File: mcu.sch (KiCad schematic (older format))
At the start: 45 parts, among them J10 debug, J7 PE10-15, J8 PD0-7, J9 USB_C_Receptacle_USB2.0, SW1 SW_MEC_5E, SW2 SW_MEC_5E, U3 STM32F407VETx, Y1 12.228Mhz

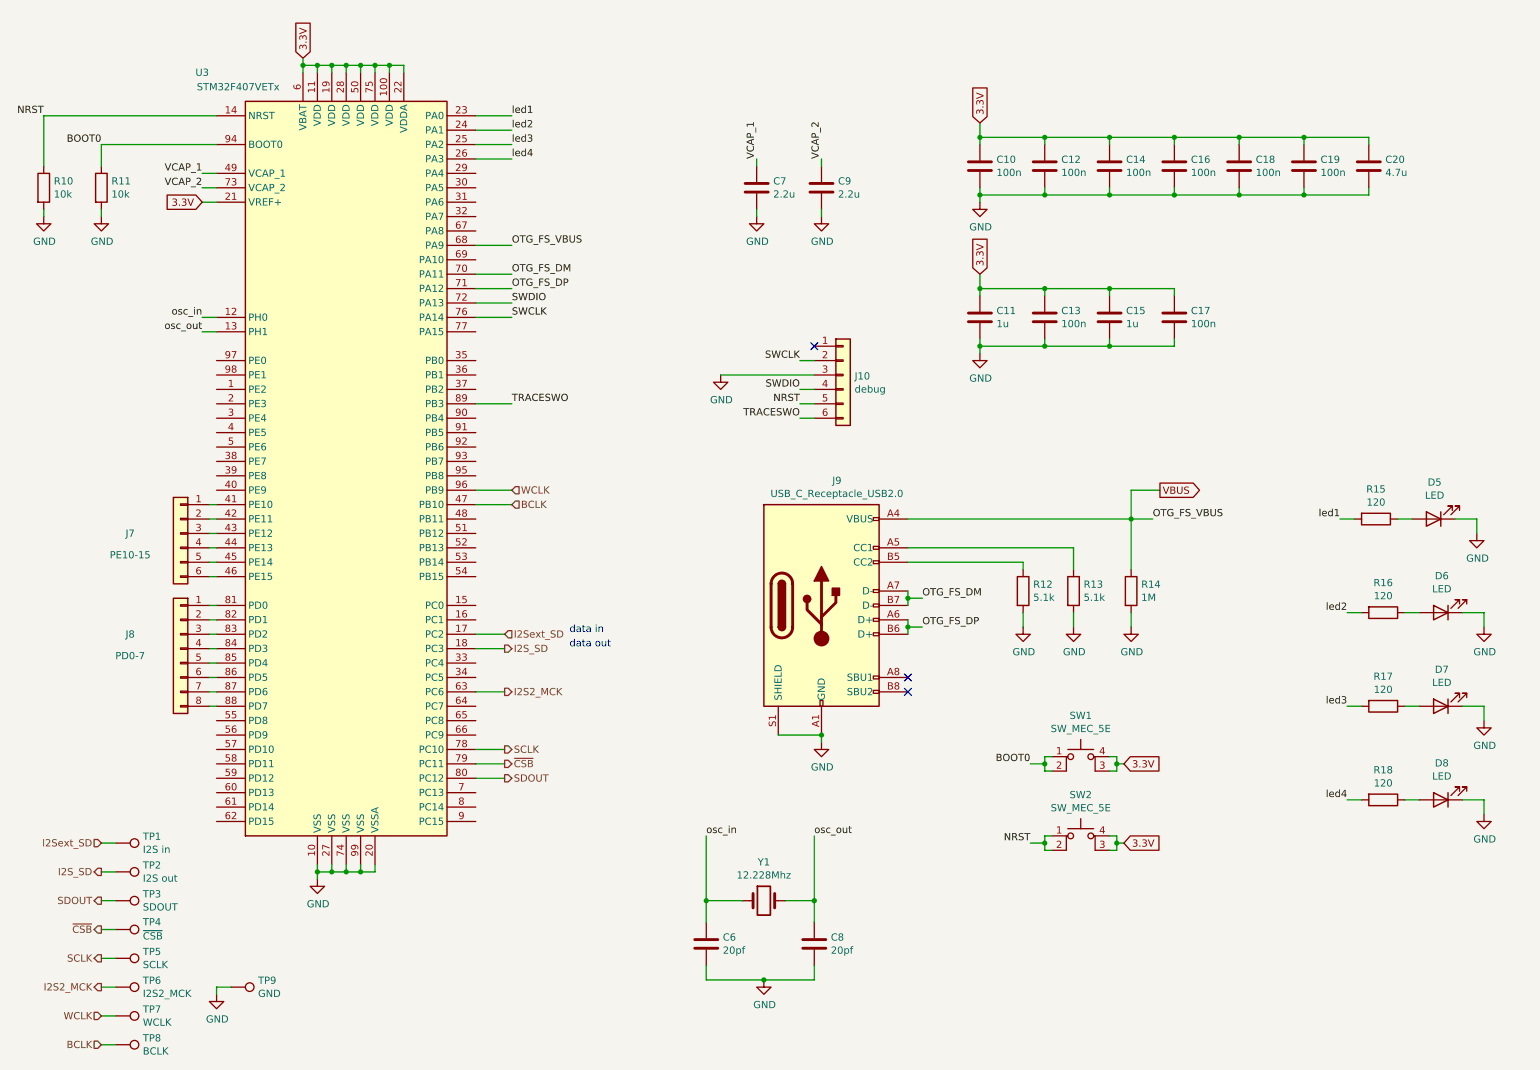
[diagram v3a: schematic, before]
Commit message: Improved probe points
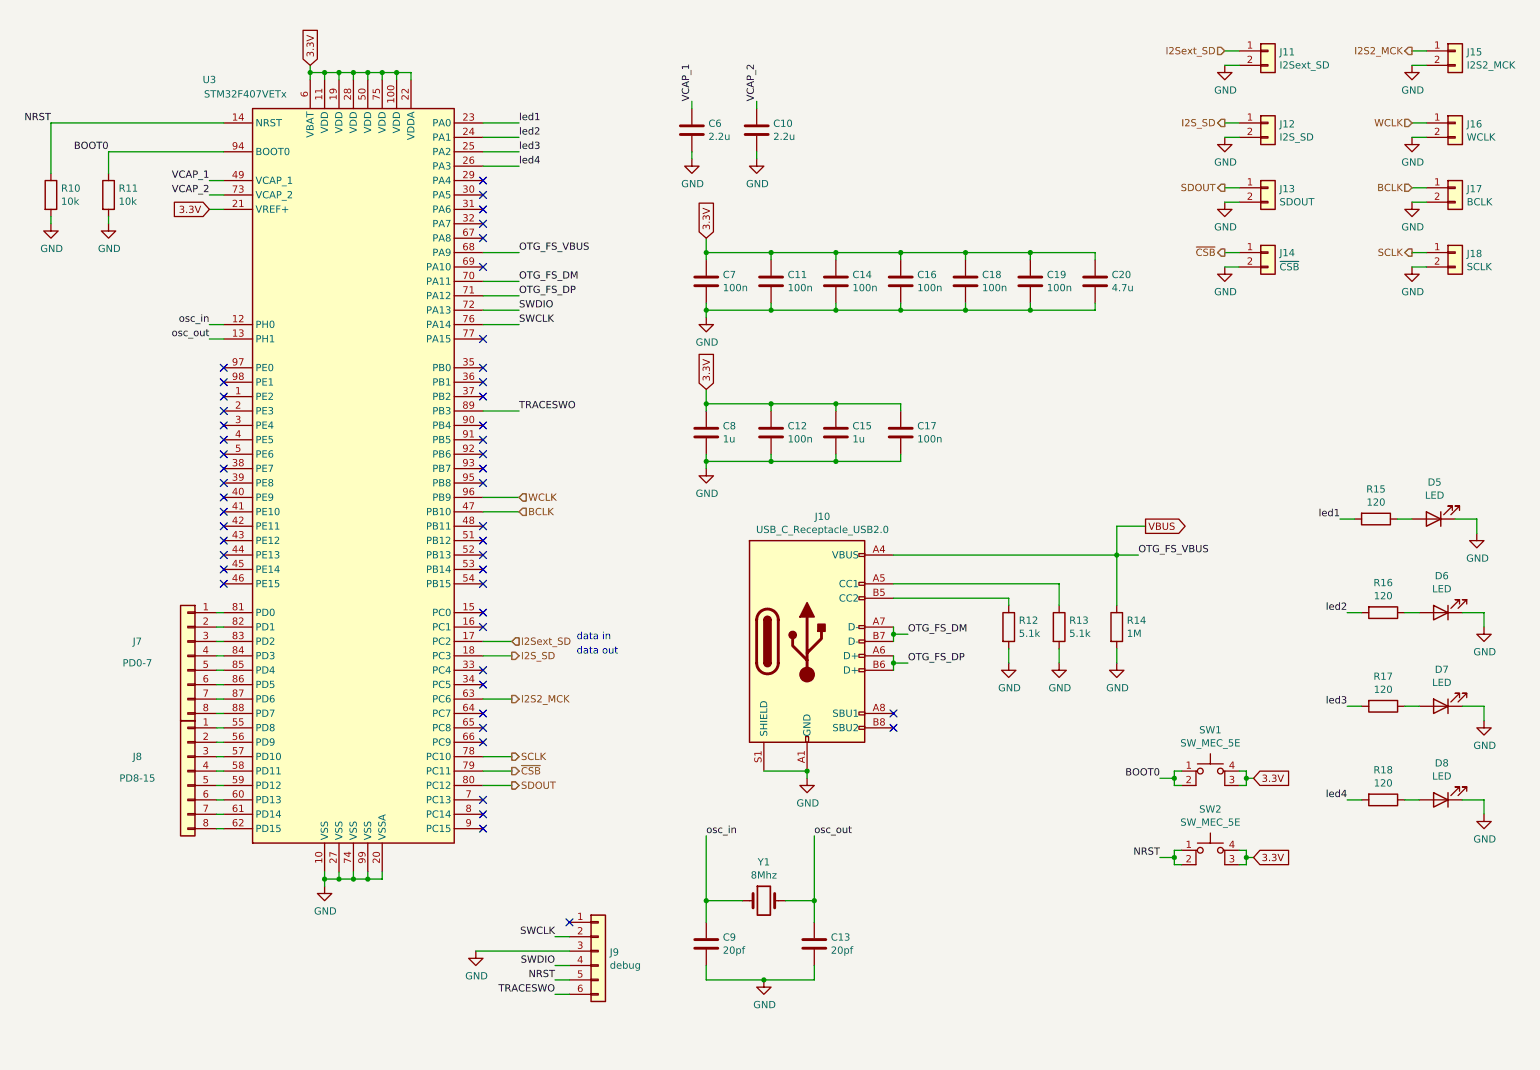
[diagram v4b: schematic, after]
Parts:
- removed J7: PE10-15, symbol Connector_Generic:Conn_01x06
- removed TP1: I2S in, symbol Connector:TestPoint
- removed TP2: I2S out, symbol Connector:TestPoint
- removed TP3: SDOUT, symbol Connector:TestPoint
- removed TP4: ~CSB, symbol Connector:TestPoint
- removed TP5: SCLK, symbol Connector:TestPoint
- removed TP6: I2S2_MCK, symbol Connector:TestPoint
- removed TP7: WCLK, symbol Connector:TestPoint
- removed TP8: BCLK, symbol Connector:TestPoint
- removed TP9: GND, symbol Connector:TestPoint
- added J11: I2Sext_SD, symbol Connector_Generic:Conn_01x02
- added J12: I2S_SD, symbol Connector_Generic:Conn_01x02
- added J13: SDOUT, symbol Connector_Generic:Conn_01x02
- added J14: ~CSB, symbol Connector_Generic:Conn_01x02
- added J15: I2S2_MCK, symbol Connector_Generic:Conn_01x02
- added J16: WCLK, symbol Connector_Generic:Conn_01x02
- added J17: BCLK, symbol Connector_Generic:Conn_01x02
- added J18: SCLK, symbol Connector_Generic:Conn_01x02
- added J8: PD8-15, symbol Connector_Generic:Conn_01x08
- Y1: value 12.228Mhz -> 8Mhz
- renumbered C9 to C10, C12 to C11, C13 to C12, C8 to C13, C7 to C6, C10 to C7, C11 to C8, C6 to C9, J9 to J10, J8 to J7, J10 to J9
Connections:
- net BCLK: now also J17.1 (Pin_1)
- net GND: now also J11.2 (Pin_2), J12.2 (Pin_2), J13.2 (Pin_2), J14.2 (Pin_2), J15.2 (Pin_2), J16.2 (Pin_2), J17.2 (Pin_2), J18.2 (Pin_2)
- net I2S2_MCK: now also J15.1 (Pin_1)
- net I2S_SD: now also J12.1 (Pin_1)
- net I2Sext_SD: now also J11.1 (Pin_1)
- net SCLK: now also J18.1 (Pin_1)
- net SDOUT: now also J13.1 (Pin_1)
- net WCLK: now also J16.1 (Pin_1)
- net ~CSB: now also J14.1 (Pin_1)
- net at U3.55 (PD8): now also J8.1 (Pin_1)
- net at U3.56 (PD9): now also J8.2 (Pin_2)
- net at U3.57 (PD10): now also J8.3 (Pin_3)
- net at U3.58 (PD11): now also J8.4 (Pin_4)
- net at U3.59 (PD12): now also J8.5 (Pin_5)
- net at U3.60 (PD13): now also J8.6 (Pin_6)
- net at U3.61 (PD14): now also J8.7 (Pin_7)
- net at U3.62 (PD15): now also J8.8 (Pin_8)
- no-connect marks 3 -> 49
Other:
- moved on the sheet: C10, C11, C12, C14, C15, C16, C17, C18, C19, C20, C6, C7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

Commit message: Assign a bunch of footprints
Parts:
- C10, C11, C12, C13, C14, C15, C16, C17, C18, C19, C20, C6, C7, C8, C9: footprint (none) -> Capacitor_SMD:C_0603_1608Metric
- D5, D6, D7, D8: footprint (none) -> LED_SMD:LED_0603_1608Metric
- J11, J12, J13, J14, J15, J16, J17, J18: footprint (none) -> Connector_PinHeader_2.54mm:PinHeader_1x02_P2.54mm_Vertical
- J7, J8: footprint (none) -> Connector_PinHeader_2.54mm:PinHeader_1x08_P2.54mm_Vertical
- J9: footprint (none) -> Connector_PinHeader_2.54mm:PinHeader_1x06_P2.54mm_Vertical
- R10, R11, R12, R13, R14, R16, R17, R18: footprint (none) -> Resistor_SMD:R_0603_1608Metric
- R15: footprint 120 -> Resistor_SMD:R_0603_1608Metric
- Y1: footprint (none) -> Crystal:Crystal_SMD_5032-2Pin_5.0x3.2mm
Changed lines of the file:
@@
 F 0 "C10" H 5815 1296 50  0000 L CNN
 F 1 "2.2u" H 5815 1205 50  0000 L CNN
-F 2 "" H 5738 1100 50  0001 C CNN
+F 2 "Capacitor_SMD:C_0603_1608Metric" H 5738 1100 50  0001 C CNN
 F 3 "~" H 5700 1250 50  0001 C CNN
 	1    5700 1250
@@
 F 0 "C6" H 5365 1296 50  0000 L CNN
 F 1 "2.2u" H 5365 1205 50  0000 L CNN
-F 2 "" H 5288 1100 50  0001 C CNN
+F 2 "Capacitor_SMD:C_0603_1608Metric" H 5288 1100 50  0001 C CNN
 F 3 "~" H 5250 1250 50  0001 C CNN
 	1    5250 1250
@@
 F 0 "C7" H 5465 2346 50  0000 L CNN
 F 1 "100n" H 5465 2255 50  0000 L CNN
-F 2 "" H 5388 2150 50  0001 C CNN
+F 2 "Capacitor_SMD:C_0603_1608Metric" H 5388 2150 50  0001 C CNN
 F 3 "~" H 5350 2300 50  0001 C CNN
 	1    5350 2300
@@
 F 0 "C11" H 5915 2346 50  0000 L CNN
 F 1 "100n" H 5915 2255 50  0000 L CNN
-F 2 "" H 5838 2150 50  0001 C CNN
+F 2 "Capacitor_SMD:C_0603_1608Metric" H 5838 2150 50  0001 C CNN
 F 3 "~" H 5800 2300 50  0001 C CNN
 	1    5800 2300
@@
 F 0 "C14" H 6365 2346 50  0000 L CNN
 F 1 "100n" H 6365 2255 50  0000 L CNN
-F 2 "" H 6288 2150 50  0001 C CNN
+F 2 "Capacitor_SMD:C_0603_1608Metric" H 6288 2150 50  0001 C CNN
 F 3 "~" H 6250 2300 50  0001 C CNN
 	1    6250 2300
@@
 F 0 "C16" H 6815 2346 50  0000 L CNN
 F 1 "100n" H 6815 2255 50  0000 L CNN
-F 2 "" H 6738 2150 50  0001 C CNN
+F 2 "Capacitor_SMD:C_0603_1608Metric" H 6738 2150 50  0001 C CNN
 F 3 "~" H 6700 2300 50  0001 C CNN
 	1    6700 2300
@@
 F 0 "C18" H 7265 2346 50  0000 L CNN
 F 1 "100n" H 7265 2255 50  0000 L CNN
-F 2 "" H 7188 2150 50  0001 C CNN
+F 2 "Capacitor_SMD:C_0603_1608Metric" H 7188 2150 50  0001 C CNN
 F 3 "~" H 7150 2300 50  0001 C CNN
 	1    7150 2300
@@
 F 0 "C19" H 7715 2346 50  0000 L CNN
 F 1 "100n" H 7715 2255 50  0000 L CNN
-F 2 "" H 7638 2150 50  0001 C CNN
+F 2 "Capacitor_SMD:C_0603_1608Metric" H 7638 2150 50  0001 C CNN
 F 3 "~" H 7600 2300 50  0001 C CNN
 	1    7600 2300
@@
 F 0 "C20" H 8165 2346 50  0000 L CNN
 F 1 "4.7u" H 8165 2255 50  0000 L CNN
-F 2 "" H 8088 2150 50  0001 C CNN
+F 2 "Capacitor_SMD:C_0603_1608Metric" H 8088 2150 50  0001 C CNN
 F 3 "~" H 8050 2300 50  0001 C CNN
 	1    8050 2300
@@
 F 0 "C8" H 5465 3396 50  0000 L CNN
 F 1 "1u" H 5465 3305 50  0000 L CNN
-F 2 "" H 5388 3200 50  0001 C CNN
+F 2 "Capacitor_SMD:C_0603_1608Metric" H 5388 3200 50  0001 C CNN
 F 3 "~" H 5350 3350 50  0001 C CNN
 	1    5350 3350
@@
 F 0 "C12" H 5915 3396 50  0000 L CNN
 F 1 "100n" H 5915 3305 50  0000 L CNN
-F 2 "" H 5838 3200 50  0001 C CNN
+F 2 "Capacitor_SMD:C_0603_1608Metric" H 5838 3200 50  0001 C CNN
 F 3 "~" H 5800 3350 50  0001 C CNN
 	1    5800 3350
@@
 F 0 "C15" H 6365 3396 50  0000 L CNN
 F 1 "1u" H 6365 3305 50  0000 L CNN
-F 2 "" H 6288 3200 50  0001 C CNN
+F 2 "Capacitor_SMD:C_0603_1608Metric" H 6288 3200 50  0001 C CNN
 F 3 "~" H 6250 3350 50  0001 C CNN
 	1    6250 3350
@@
 F 0 "C17" H 6815 3396 50  0000 L CNN
 F 1 "100n" H 6815 3305 50  0000 L CNN
-F 2 "" H 6738 3200 50  0001 C CNN
+F 2 "Capacitor_SMD:C_0603_1608Metric" H 6738 3200 50  0001 C CNN
 F 3 "~" H 6700 3350 50  0001 C CNN
 	1    6700 3350
@@
 F 0 "C9" H 5465 6946 50  0000 L CNN
 F 1 "20pf" H 5465 6855 50  0000 L CNN
-F 2 "" H 5388 6750 50  0001 C CNN
+F 2 "Capacitor_SMD:C_0603_1608Metric" H 5388 6750 50  0001 C CNN
 F 3 "~" H 5350 6900 50  0001 C CNN
 	1    5350 6900
@@
 F 0 "C13" H 6215 6946 50  0000 L CNN
 F 1 "20pf" H 6215 6855 50  0000 L CNN
-F 2 "" H 6138 6750 50  0001 C CNN
+F 2 "Capacitor_SMD:C_0603_1608Metric" H 6138 6750 50  0001 C CNN
 F 3 "~" H 6100 6900 50  0001 C CNN
 	1    6100 6900
@@
 F 0 "D5" H 10393 3695 50  0000 C CNN
 F 1 "LED" H 10393 3786 50  0000 C CNN
-F 2 "" H 10400 3950 50  0001 C CNN
+F 2 "LED_SMD:LED_0603_1608Metric" H 10400 3950 50  0001 C CNN
 F 3 "~" H 10400 3950 50  0001 C CNN
 	1    10400 3950
@@
 F 0 "R15" V 9793 3950 50  0000 C CNN
 F 1 "120" V 9884 3950 50  0000 C CNN
-F 2 "120" V 9930 3950 50  0001 C CNN
+F 2 "Resistor_SMD:R_0603_1608Metric" V 9930 3950 50  0001 C CNN
 F 3 "~" H 10000 3950 50  0001 C CNN
 	1    10000 3950
@@
 F 0 "D6" H 10443 4345 50  0000 C CNN
 F 1 "LED" H 10443 4436 50  0000 C CNN
-F 2 "" H 10450 4600 50  0001 C CNN
+F 2 "LED_SMD:LED_0603_1608Metric" H 10450 4600 50  0001 C CNN
 F 3 "~" H 10450 4600 50  0001 C CNN
 	1    10450 4600
@@
 F 0 "R16" V 9843 4600 50  0000 C CNN
 F 1 "120" V 9934 4600 50  0000 C CNN
-F 2 "" V 9980 4600 50  0001 C CNN
+F 2 "Resistor_SMD:R_0603_1608Metric" V 9980 4600 50  0001 C CNN
 F 3 "~" H 10050 4600 50  0001 C CNN
 	1    10050 4600
@@
 F 0 "D7" H 10443 4995 50  0000 C CNN
 F 1 "LED" H 10443 5086 50  0000 C CNN
-F 2 "" H 10450 5250 50  0001 C CNN
+F 2 "LED_SMD:LED_0603_1608Metric" H 10450 5250 50  0001 C CNN
 F 3 "~" H 10450 5250 50  0001 C CNN
 	1    10450 5250
@@
 F 0 "R17" V 9843 5250 50  0000 C CNN
 F 1 "120" V 9934 5250 50  0000 C CNN
-F 2 "" V 9980 5250 50  0001 C CNN
+F 2 "Resistor_SMD:R_0603_1608Metric" V 9980 5250 50  0001 C CNN
 F 3 "~" H 10050 5250 50  0001 C CNN
 	1    10050 5250
@@
 F 0 "D8" H 10443 5645 50  0000 C CNN
 F 1 "LED" H 10443 5736 50  0000 C CNN
-F 2 "" H 10450 5900 50  0001 C CNN
+F 2 "LED_SMD:LED_0603_1608Metric" H 10450 5900 50  0001 C CNN
 F 3 "~" H 10450 5900 50  0001 C CNN
 	1    10450 5900
@@
 F 0 "R18" V 9843 5900 50  0000 C CNN
 F 1 "120" V 9934 5900 50  0000 C CNN
-F 2 "" V 9980 5900 50  0001 C CNN
+F 2 "Resistor_SMD:R_0603_1608Metric" V 9980 5900 50  0001 C CNN
 F 3 "~" H 10050 5900 50  0001 C CNN
 	1    10050 5900
@@
 F 0 "R12" H 7520 4746 50  0000 L CNN
 F 1 "5.1k" H 7520 4655 50  0000 L CNN
-F 2 "" V 7380 4700 50  0001 C CNN
+F 2 "Resistor_SMD:R_0603_1608Metric" V 7380 4700 50  0001 C CNN
 F 3 "~" H 7450 4700 50  0001 C CNN
 	1    7450 4700
@@
 F 0 "R13" H 7870 4746 50  0000 L CNN
 F 1 "5.1k" H 7870 4655 50  0000 L CNN
-F 2 "" V 7730 4700 50  0001 C CNN
+F 2 "Resistor_SMD:R_0603_1608Metric" V 7730 4700 50  0001 C CNN
 F 3 "~" H 7800 4700 50  0001 C CNN
 	1    7800 4700
@@
 F 0 "R14" H 8270 4746 50  0000 L CNN
 F 1 "1M" H 8270 4655 50  0000 L CNN
-F 2 "" V 8130 4700 50  0001 C CNN
+F 2 "Resistor_SMD:R_0603_1608Metric" V 8130 4700 50  0001 C CNN
 F 3 "~" H 8200 4700 50  0001 C CNN
 	1    8200 4700
@@
 F 0 "J9" H 4680 6942 50  0000 L CNN
 F 1 "debug" H 4680 6851 50  0000 L CNN
-F 2 "" H 4600 6950 50  0001 C CNN
+F 2 "Connector_PinHeader_2.54mm:PinHeader_1x06_P2.54mm_Vertical" H 4600 6950 50  0001 C CNN
 F 3 "~" H 4600 6950 50  0001 C CNN
 	1    4600 6950
@@
 F 0 "Y1" H 5750 6868 50  0000 C CNN
 F 1 "8Mhz" H 5750 6777 50  0000 C CNN
-F 2 "" H 5750 6600 50  0001 C CNN
+F 2 "Crystal:Crystal_SMD_5032-2Pin_5.0x3.2mm" H 5750 6600 50  0001 C CNN
 F 3 "~" H 5750 6600 50  0001 C CNN
 	1    5750 6600
@@
 F 0 "J8" H 2100 5800 50  0000 C CNN
 F 1 "PD8-15" H 2100 5650 50  0000 C CNN
-F 2 "" H 1750 5700 50  0001 C CNN
+F 2 "Connector_PinHeader_2.54mm:PinHeader_1x08_P2.54mm_Vertical" H 1750 5700 50  0001 C CNN
 F 3 "~" H 1750 5700 50  0001 C CNN
 	1    1750 5700
@@
 F 0 "J7" H 2100 5000 50  0000 C CNN
 F 1 "PD0-7" H 2100 4850 50  0000 C CNN
-F 2 "" H 1750 4900 50  0001 C CNN
+F 2 "Connector_PinHeader_2.54mm:PinHeader_1x08_P2.54mm_Vertical" H 1750 4900 50  0001 C CNN
 F 3 "~" H 1750 4900 50  0001 C CNN
 	1    1750 4900
@@
 F 0 "R10" H 870 1746 50  0000 L CNN
 F 1 "10k" H 870 1655 50  0000 L CNN
-F 2 "" V 730 1700 50  0001 C CNN
+F 2 "Resistor_SMD:R_0603_1608Metric" V 730 1700 50  0001 C CNN
 F 3 "~" H 800 1700 50  0001 C CNN
 	1    800  1700
@@
 F 0 "R11" H 1270 1746 50  0000 L CNN
 F 1 "10k" H 1270 1655 50  0000 L CNN
-F 2 "" V 1130 1700 50  0001 C CNN
+F 2 "Resistor_SMD:R_0603_1608Metric" V 1130 1700 50  0001 C CNN
 F 3 "~" H 1200 1700 50  0001 C CNN
 	1    1200 1700
@@
 F 0 "J11" H 9330 692 50  0000 L CNN
 F 1 "I2Sext_SD" H 9330 601 50  0000 L CNN
-F 2 "" H 9250 700 50  0001 C CNN
+F 2 "Connector_PinHeader_2.54mm:PinHeader_1x02_P2.54mm_Vertical" H 9250 700 50  0001 C CNN
 F 3 "~" H 9250 700 50  0001 C CNN
 	1    9250 700
@@
 F 0 "J12" H 9330 1192 50  0000 L CNN
 F 1 "I2S_SD" H 9330 1101 50  0000 L CNN
-F 2 "" H 9250 1200 50  0001 C CNN
+F 2 "Connector_PinHeader_2.54mm:PinHeader_1x02_P2.54mm_Vertical" H 9250 1200 50  0001 C CNN
 F 3 "~" H 9250 1200 50  0001 C CNN
 	1    9250 1200
@@
 F 0 "J13" H 9330 1642 50  0000 L CNN
 F 1 "SDOUT" H 9330 1551 50  0000 L CNN
-F 2 "" H 9250 1650 50  0001 C CNN
+F 2 "Connector_PinHeader_2.54mm:PinHeader_1x02_P2.54mm_Vertical" H 9250 1650 50  0001 C CNN
 F 3 "~" H 9250 1650 50  0001 C CNN
 	1    9250 1650
@@
 F 0 "J14" H 9330 2098 50  0000 L CNN
 F 1 "~CSB" H 9330 2000 50  0000 L CNN
-F 2 "" H 9250 2100 50  0001 C CNN
+F 2 "Connector_PinHeader_2.54mm:PinHeader_1x02_P2.54mm_Vertical" H 9250 2100 50  0001 C CNN
 F 3 "~" H 9250 2100 50  0001 C CNN
 	1    9250 2100
@@
 F 0 "J18" H 10630 2092 50  0000 L CNN
 F 1 "SCLK" H 10630 2001 50  0000 L CNN
-F 2 "" H 10550 2100 50  0001 C CNN
+F 2 "Connector_PinHeader_2.54mm:PinHeader_1x02_P2.54mm_Vertical" H 10550 2100 50  0001 C CNN
 F 3 "~" H 10550 2100 50  0001 C CNN
 	1    10550 2100
@@
 F 0 "J15" H 10630 692 50  0000 L CNN
 F 1 "I2S2_MCK" H 10630 601 50  0000 L CNN
-F 2 "" H 10550 700 50  0001 C CNN
+F 2 "Connector_PinHeader_2.54mm:PinHeader_1x02_P2.54mm_Vertical" H 10550 700 50  0001 C CNN
 F 3 "~" H 10550 700 50  0001 C CNN
 	1    10550 700
@@
 F 0 "J16" H 10630 1192 50  0000 L CNN
 F 1 "WCLK" H 10630 1101 50  0000 L CNN
-F 2 "" H 10550 1200 50  0001 C CNN
+F 2 "Connector_PinHeader_2.54mm:PinHeader_1x02_P2.54mm_Vertical" H 10550 1200 50  0001 C CNN
 F 3 "~" H 10550 1200 50  0001 C CNN
 	1    10550 1200
@@
 F 0 "J17" H 10630 1642 50  0000 L CNN
 F 1 "BCLK" H 10630 1551 50  0000 L CNN
-F 2 "" H 10550 1650 50  0001 C CNN
+F 2 "Connector_PinHeader_2.54mm:PinHeader_1x02_P2.54mm_Vertical" H 10550 1650 50  0001 C CNN
 F 3 "~" H 10550 1650 50  0001 C CNN
 	1    10550 1650
